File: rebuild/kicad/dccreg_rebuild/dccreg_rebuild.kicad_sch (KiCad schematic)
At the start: 0 parts

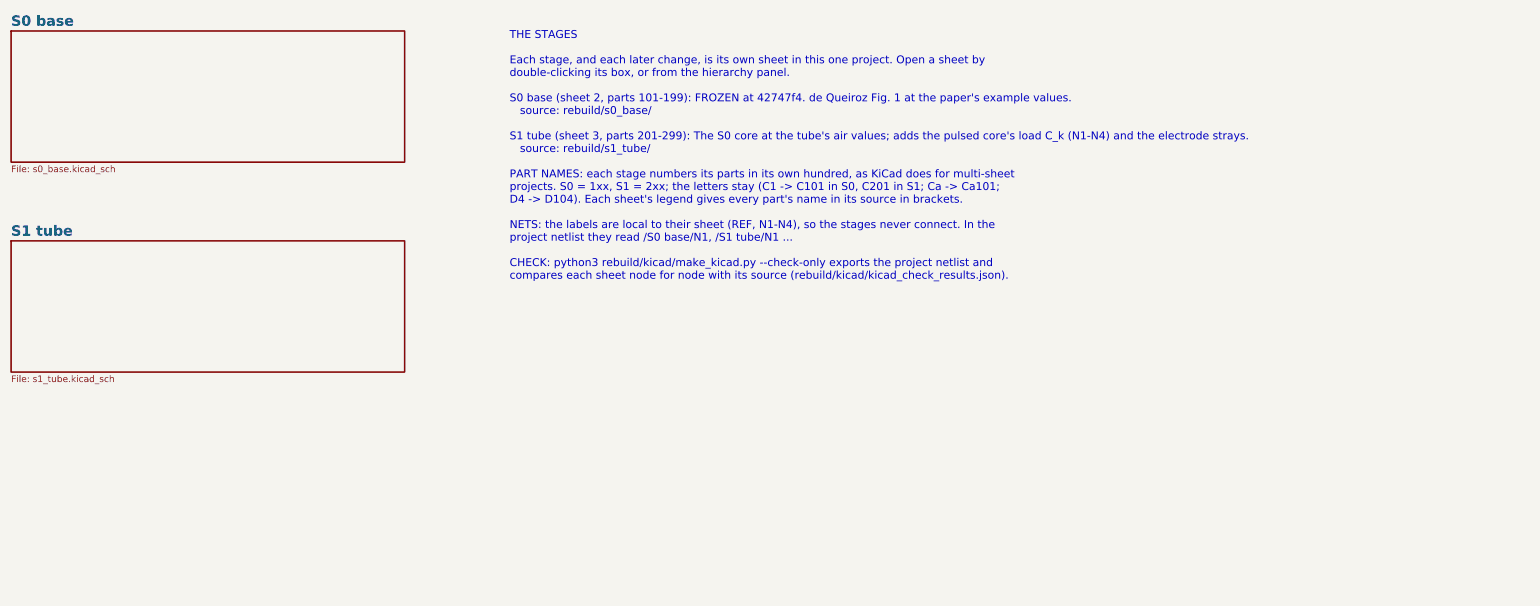
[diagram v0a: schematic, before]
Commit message: feat(rebuild): S1b, the zener clamp on the S1 core
The designer chose the zener (avalanche) clamp as the voltage limit for
now ("not using it on the physical bench is just matter of disconnecting
it"), at 13.13 kV with one string per node. The other options stay on
file for later. The decision is recorded in ledger section 2.3 and
rebuild/README.md; the PDFs are not rebuilt.

rebuild/s1_tube/s1b_clamp.py puts two 66 x 200 V strings (1.5KE200A
class) on the S1 core, in ngspice with real HV sticks:
- the nodes hold at 13.13 kV, 1.50x under the gap's 19.70 kV breakdown;
- each string takes 0.79 W (12 mW per part); 1.57 W together, against
  the ideal limit's 1.63 W;
- the +-5 % spread keeps the margin at >= 1.43x; a mismatched pair makes
  the core field asymmetric;
- self-start: <= 1 V with typical leakage, ~0.7 kV with hot strings,
  ~1.3 kV with everything hot.

The KiCad project gains the sheet S1b clamp (parts 3xx). Its netlist
matches the study's TOPOLOGY, the ERC is clean, and the S0 and S1 sheets
are unchanged.

Co-Authored-By: Claude Opus 5.5 <noreply@anthropic.com>
Claude-Session: https://claude.ai/code/session_01EZwGpTFL1hyaEya41kJtBw
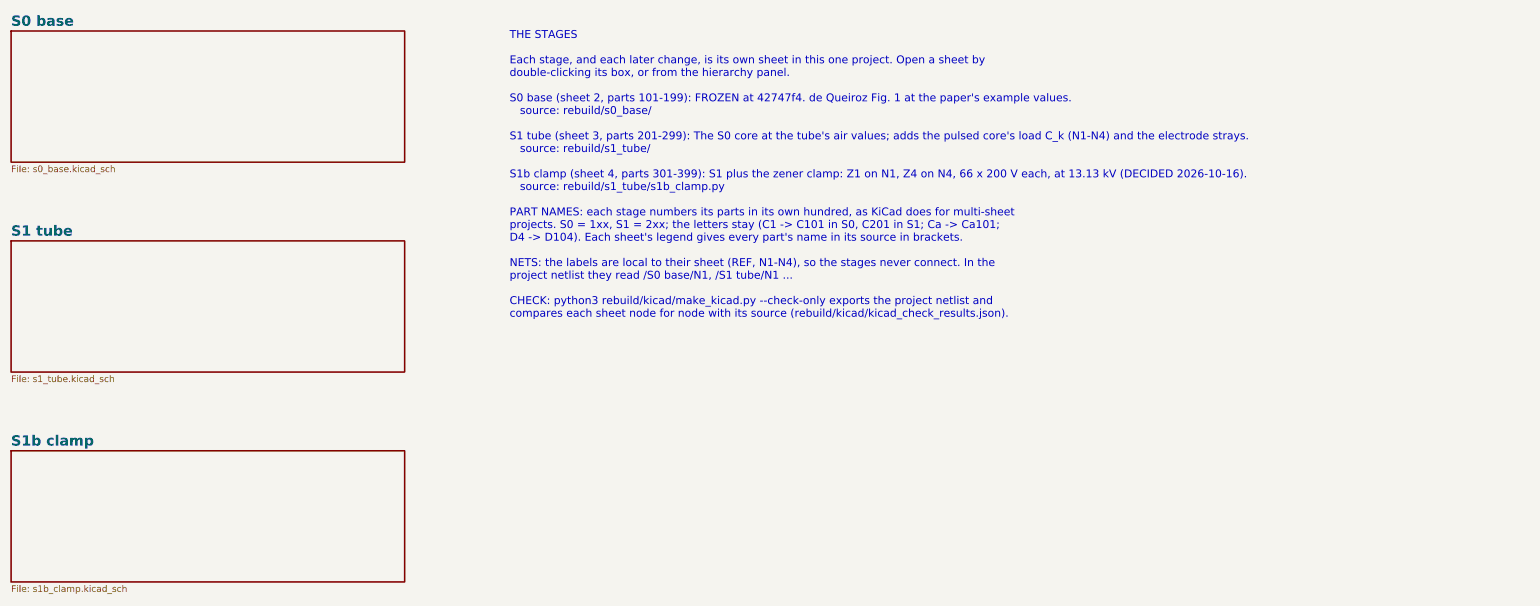
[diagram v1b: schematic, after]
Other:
- added sheet S1b clamp (s1b_clamp.kicad_sch)
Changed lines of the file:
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@@
 		)
 	)
-	(text "THE STAGES\n\nEach stage, and each later change, is its own sheet in this one project. Open a sheet by\ndouble-clicking its box, or from the hierarchy panel.\n\nS0 base (sheet 2, parts 101-199): FROZEN at 42747f4. de Queiroz Fig. 1 at the paper's example values.\n   source: rebuild/s0_base/\n\nS1 tube (sheet 3, parts 201-299): The S0 core at the tube's air values; adds the pulsed core's load C_k (N1-N4) and the electrode strays.\n   source: rebuild/s1_tube/\n\nPART NAMES: each stage numbers its parts in its own hundred, as KiCad does for multi-sheet\nprojects. S0 = 1xx, S1 = 2xx; the letters stay (C1 -> C101 in S0, C201 in S1; Ca -> Ca101;\nD4 -> D104). Each sheet's legend gives every part's name in its source in brackets.\n\nNETS: the labels are local to their sheet (REF, N1-N4), so the stages never connect. In the\nproject netlist they read /S0 base/N1, /S1 tube/N1 ...\n\nCHECK: python3 rebuild/kicad/make_kicad.py --check-only exports the project netlist and\ncompares each sheet node for node with its source (rebuild/kicad/kicad_check_results.json)."
+	(sheet
+		(at 30.48 132.08)
+		(size 76.2 25.4)
+		(exclude_from_sim no)
+		(in_bom yes)
+		(on_board yes)
+		(dnp no)
+		(stroke
+			(width 0.3)
+			(type solid)
+		)
+		(fill
+			(color 0 0 0 0)
+		)
+		(property "Sheetname" "S1b clamp"
+			(at 30.48 131.32 0)
+			(show_name no)
+			(do_not_autoplace no)
+			(effects
+				(font
+					(size 2 2)
+					(bold yes)
+				)
+				(justify left bottom)
+			)
+		)
+		(property "Sheetfile" "s1b_clamp.kicad_sch"
+			(at 30.48 158.08 0)
+			(show_name no)
+			(do_not_autoplace no)
+			(effects
+				(font
+					(size 1.27 1.27)
+				)
+				(justify left top)
+			)
+		)
+		(instances
+			(project "dccreg_rebuild"
+				(path "/18804d6c-8df5-516d-ac91-9d2744fe7221"
+					(page "4")
+				)
+			)
+		)
+	)
+	(text "THE STAGES\n\nEach stage, and each later change, is its own sheet in this one project. Open a sheet by\ndouble-clicking its box, or from the hierarchy panel.\n\nS0 base (sheet 2, parts 101-199): FROZEN at 42747f4. de Queiroz Fig. 1 at the paper's example values.\n   source: rebuild/s0_base/\n\nS1 tube (sheet 3, parts 201-299): The S0 core at the tube's air values; adds the pulsed core's load C_k (N1-N4) and the electrode strays.\n   source: rebuild/s1_tube/\n\nS1b clamp (sheet 4, parts 301-399): S1 plus the zener clamp: Z1 on N1, Z4 on N4, 66 x 200 V each, at 13.13 kV (DECIDED 2026-10-16).\n   source: rebuild/s1_tube/s1b_clamp.py\n\nPART NAMES: each stage numbers its parts in its own hundred, as KiCad does for multi-sheet\nprojects. S0 = 1xx, S1 = 2xx; the letters stay (C1 -> C101 in S0, C201 in S1; Ca -> Ca101;\nD4 -> D104). Each sheet's legend gives every part's name in its source in brackets.\n\nNETS: the labels are local to their sheet (REF, N1-N4), so the stages never connect. In the\nproject netlist they read /S0 base/N1, /S1 tube/N1 ...\n\nCHECK: python3 rebuild/kicad/make_kicad.py --check-only exports the project netlist and\ncompares each sheet node for node with its source (rebuild/kicad/kicad_check_results.json)."
 		(exclude_from_sim yes)
 		(at 127 50.8 0)
